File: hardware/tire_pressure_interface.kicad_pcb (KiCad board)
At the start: 2 copper layers, 98 x 40.1 mm, 82 parts, among them IC1 TPS54202HDDCR, J3 FTSH-107-01-L-D-K, J4 Conn_02x02_Counter_Clockwise, J5 Micro_SD_Card_Det1, Q1 SI2347DS-T1-GE3, T1 TP_+3V3, T10 TP_+5V, T11 TP_+5V, T3 TP_VCC, T8 TP_VCC, T9 TP_+3V3, U1 STM32G0C1KCTxN, U2 LM1117-3.3, U3 XIAO-ESP32-S3-DIP, U7 ADM3057ExRW

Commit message: pcb routing
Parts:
- moved T1 0.24 mm to (108.4, 114.0)
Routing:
- net GND: track 0.00 -> 115.7 mm, vias 0 -> 13
- net +3V3: track 0.00 -> 98.4 mm, vias 0 -> 13
- net /STM32/STM_VCC: track 0.00 -> 54.7 mm, vias 0 -> 5
- net /CAN_BUS/GND_CAN_ISO1: track 0.00 -> 51.2 mm, vias 0 -> 2
- net /Connectors/CAN.H: track 0.00 -> 48.2 mm
- net /Connectors/CAN.L: track 0.00 -> 47.8 mm
- net +5V: track 0.00 -> 46.8 mm
- net /TX: track 0.00 -> 45.5 mm, vias 0 -> 4
- net /RX: track 0.00 -> 44.6 mm, vias 0 -> 2
- net /Connectors/RST: track 0.00 -> 44.2 mm
- net /Power/VCC_IN: track 0.00 -> 43.3 mm, vias 0 -> 2
- net (no net): track 0.00 -> 38.1 mm
- net /CAN_BUS/CAN_RX: track 0.00 -> 32.8 mm
- net /CAN_BUS/STBY_CAN_1: track 0.00 -> 29.4 mm, vias 0 -> 2
- net /STM32/LED.ERR: track 0.00 -> 27.4 mm, vias 0 -> 2
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- added copper zone on B.Cu, net GND
- added copper zone on F.Cu, net GND

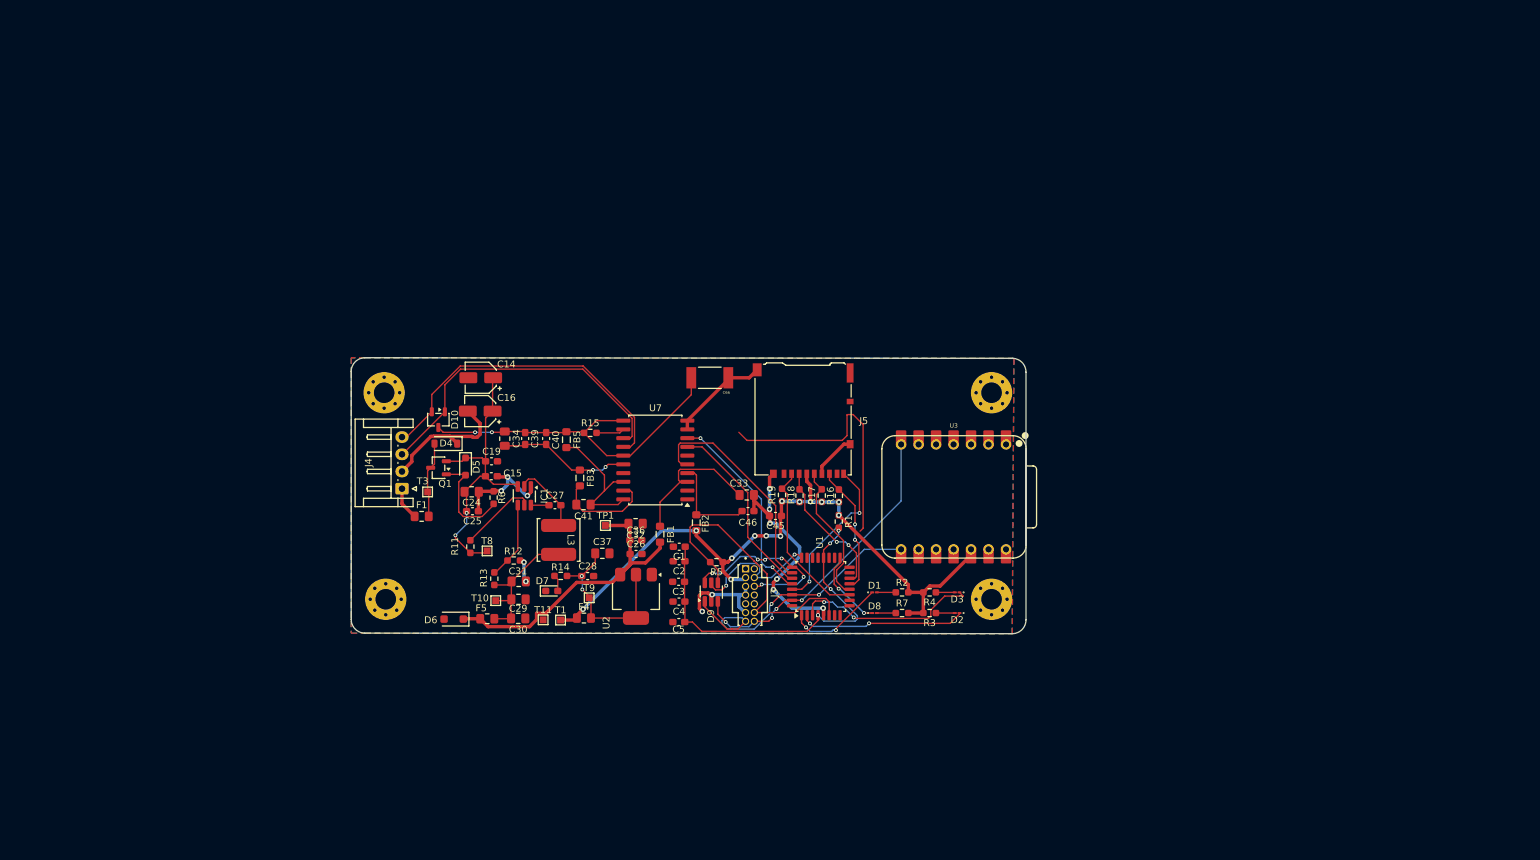
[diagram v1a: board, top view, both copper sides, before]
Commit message: power section routing
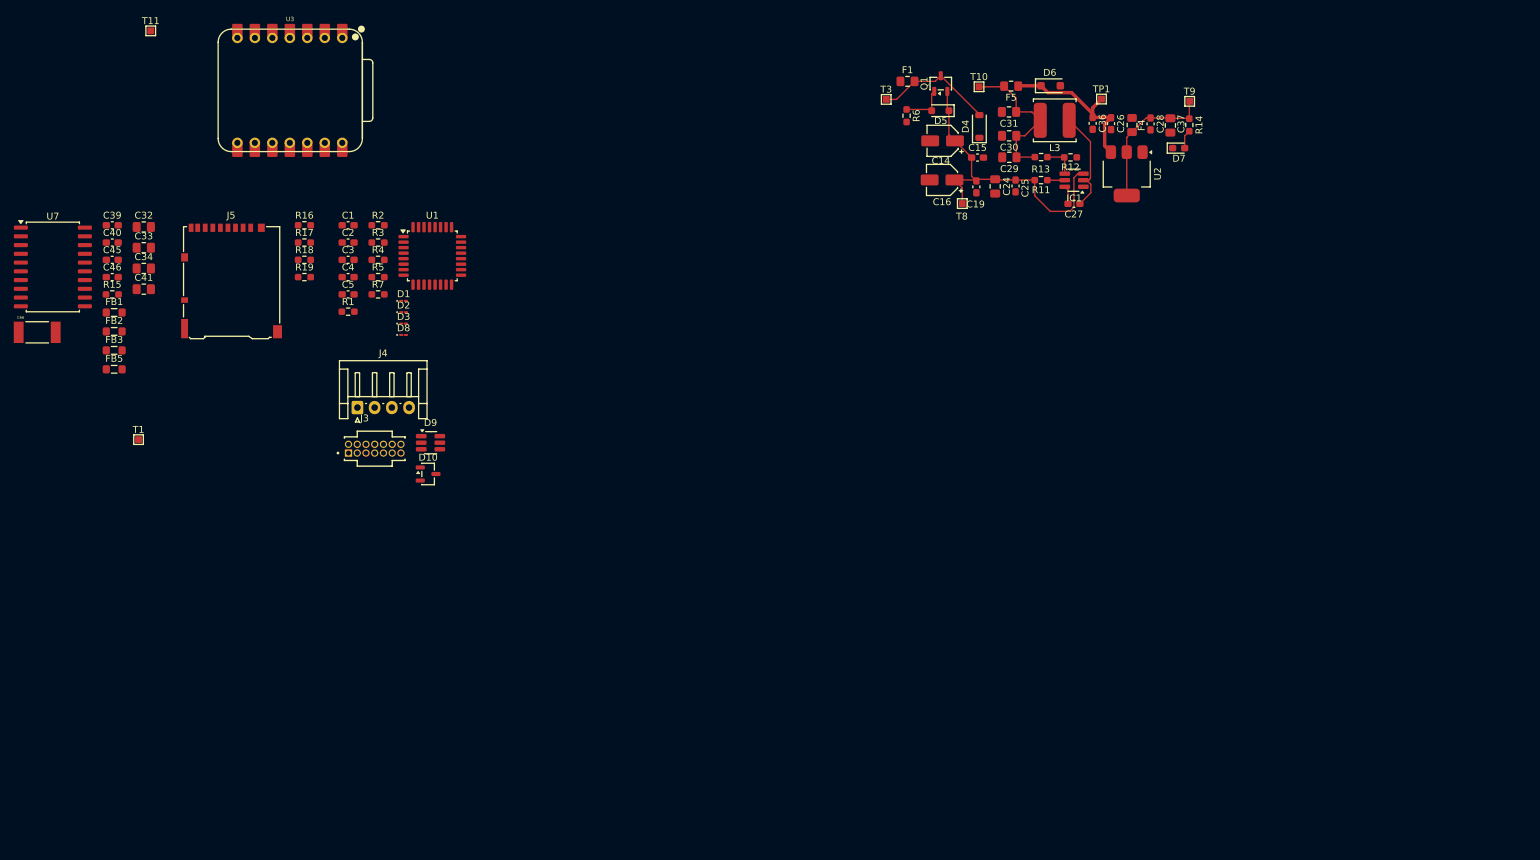
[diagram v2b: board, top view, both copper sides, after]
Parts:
- removed REF** (x4): MountingHole_3mm_Pad_Via, MountingHole:MountingHole_3mm_Pad_Via
- moved D6 116.3 mm to (179.6, 36.4), turned to 0 degrees
- moved T9 113.2 mm to (199.8, 38.7)
- moved U3 113.1 mm to (69.1, 37.1)
- moved R14 112.4 mm to (199.7, 42.1), turned to -90 degrees
- moved D7 111.5 mm to (198.2, 45.5)
- moved F5 108.5 mm to (173.8, 36.5), turned to 180 degrees
- moved F4 107.1 mm to (191.4, 42.1), turned to -90 degrees
- moved C28 104.9 mm to (194.1, 42.0), turned to -90 degrees
- moved C37 103.3 mm to (197.0, 42.2), turned to -90 degrees
- moved C45 103.3 mm to (43.3, 61.7), turned to 0 degrees
- moved T11 102.8 mm to (48.9, 28.4)
- moved T10 102.5 mm to (169.2, 36.6)
- moved R13 100.3 mm to (178.2, 46.8), turned to 180 degrees
- moved C30 100.0 mm to (173.6, 43.7), turned to 180 degrees
- moved R12 99.8 mm to (182.5, 46.8)
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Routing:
- net GND: track 115.7 -> 0.00 mm, vias 13 -> 0
- net +3V3: track 98.4 -> 0.00 mm, vias 13 -> 0
- net /STM32/STM_VCC: track 54.7 -> 0.00 mm, vias 5 -> 0
- net /CAN_BUS/GND_CAN_ISO1: track 51.2 -> 0.00 mm, vias 2 -> 0
- net /Connectors/CAN.H: track 48.2 -> 0.00 mm
- net /Connectors/CAN.L: track 47.8 -> 0.00 mm
- net /TX: track 45.5 -> 0.00 mm, vias 4 -> 0
- net /RX: track 44.6 -> 0.00 mm, vias 2 -> 0
- net /Connectors/RST: track 44.2 -> 0.00 mm
- net (no net): track 38.1 -> 0.00 mm
- net /CAN_BUS/CAN_RX: track 32.8 -> 0.00 mm
- net /CAN_BUS/STBY_CAN_1: track 29.4 -> 0.00 mm, vias 2 -> 0
- net /STM32/LED.ERR: track 27.4 -> 0.00 mm, vias 2 -> 0
- net /CAN_BUS/CAN_TX: track 26.9 -> 0.00 mm
- net /Connectors/SWCLK: track 25.8 -> 0.00 mm, vias 6 -> 0
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- removed copper zone on B.Cu, net GND
- removed copper zone on F.Cu, net GND
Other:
- board outline removed
- copper layers 2 -> 4

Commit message: power section and isocan layout
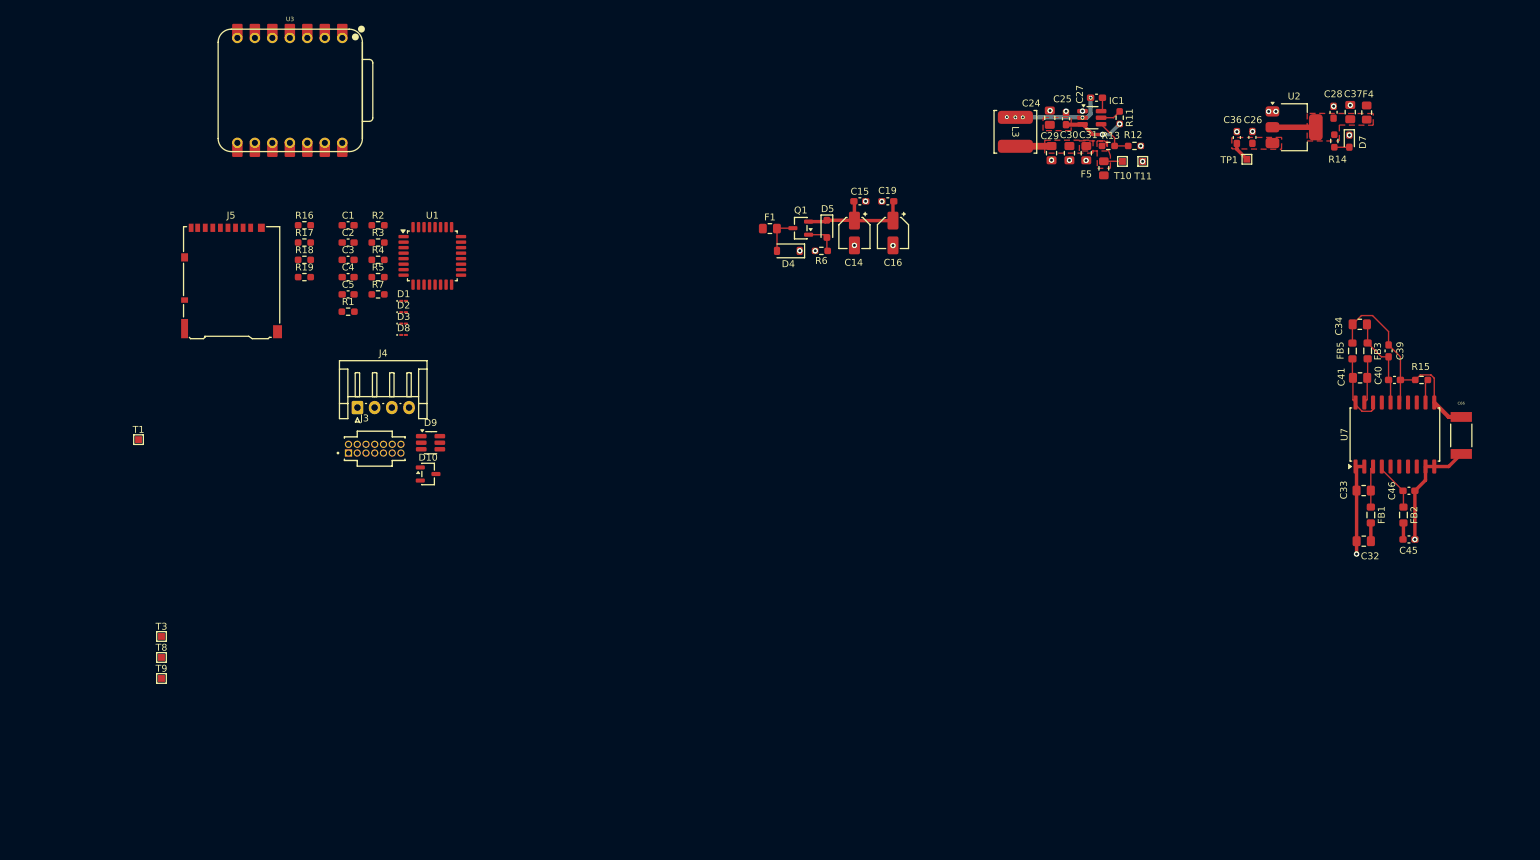
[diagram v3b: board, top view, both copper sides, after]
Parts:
- removed D6: SKL34, Diode_SMD:D_SOD-123F
- moved C66 207.4 mm to (239.2, 87.2), turned to 90 degrees
- moved U7 196.5 mm to (229.6, 87.1), turned to 90 degrees
- moved C45 192.7 mm to (231.6, 102.3)
- moved C46 190.9 mm to (231.6, 95.2)
- moved R15 190.6 mm to (233.5, 79.1)
- moved FB2 189.2 mm to (230.8, 98.8), turned to -90 degrees
- moved C40 187.3 mm to (229.5, 79.1)
- moved C39 186.3 mm to (228.7, 74.9), turned to -90 degrees
- moved FB1 184.9 mm to (226.1, 98.8), turned to -90 degrees
- moved C32 183.0 mm to (225.1, 102.6)
- moved FB3 182.1 mm to (225.6, 74.9), turned to -90 degrees
- moved C33 180.7 mm to (225.1, 95.2)
- moved FB5 179.9 mm to (223.4, 74.9), turned to -90 degrees
- moved C41 177.1 mm to (224.5, 78.8)
- moved C34 176.8 mm to (224.5, 71.1)
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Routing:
- net GND: track 0.00 -> 36.5 mm, vias 0 -> 23
- net /CAN_BUS/GND_CAN_ISO1: track 0.00 -> 34.3 mm
- net +5V: track 24.7 -> 5.56 mm
- net /Power/VCC_IN: track 45.6 -> 27.1 mm, vias 0 -> 2
- net /Power/+5V_OUT: track 23.0 -> 7.98 mm
- net /Power/VO_+3.3V: track 21.3 -> 6.36 mm
- net Net-(U7-VISOIN): track 0.00 -> 13.4 mm
- net /Power/RPP_D: track 17.4 -> 5.58 mm
- net Net-(C41-Pad1): track 0.00 -> 10.9 mm
- net Net-(U7-VIO): track 0.00 -> 7.20 mm
- net Net-(U7-VISOOUT): track 0.00 -> 6.55 mm
- net Net-(U7-VCC): track 0.00 -> 6.03 mm
- net Net-(U7-RS): track 0.00 -> 3.42 mm
- net +3V3: track 0.00 -> 2.43 mm
- net /Power/RPP_G: track 6.68 -> 4.82 mm
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- added copper zone on F.Cu, net +5V
- added copper zone on F.Cu, net /Power/+5V_OUT
- added copper zone on F.Cu, net /Power/VCC_IN
- added copper zone on F.Cu, net /Power/VO_+3.3V

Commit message: STM32G0 and micro sd layout
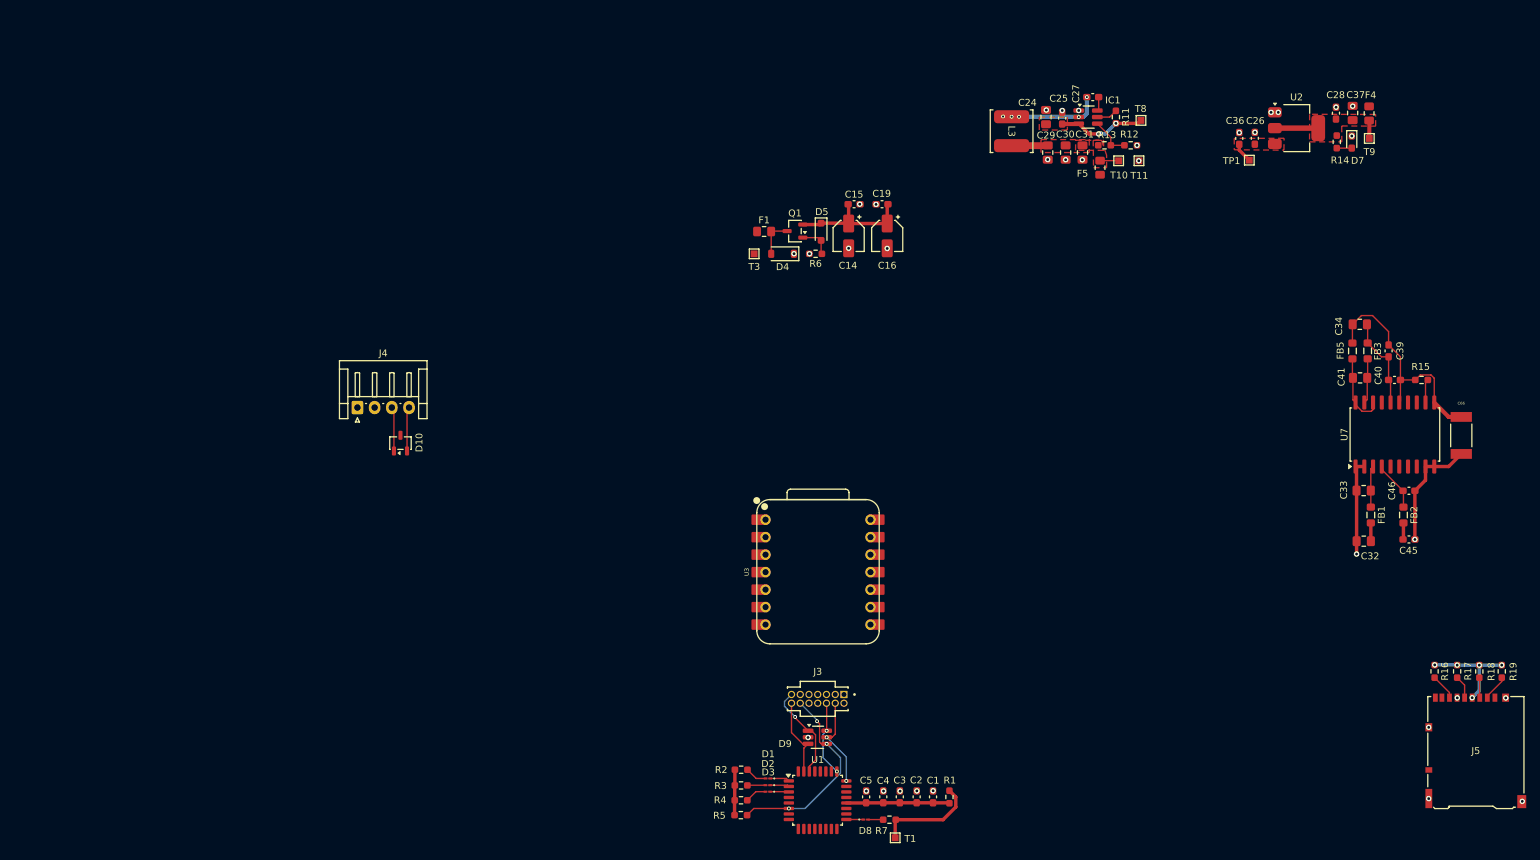
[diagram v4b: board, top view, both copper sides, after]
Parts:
- moved J5 193.2 mm to (241.3, 133.0)
- moved T9 192.2 mm to (225.9, 44.1)
- moved R19 183.1 mm to (245.1, 121.5), turned to -90 degrees
- moved R18 180.8 mm to (241.8, 121.5), turned to -90 degrees
- moved R17 178.7 mm to (238.6, 121.5), turned to -90 degrees
- moved R16 176.5 mm to (235.3, 121.5), turned to -90 degrees
- moved T8 162.3 mm to (192.7, 41.4)
- moved T1 124.2 mm to (157.0, 145.7)
- moved C1 118.8 mm to (162.5, 139.7), turned to 90 degrees
- moved C2 115.3 mm to (160.1, 139.7), turned to 90 degrees
- moved R1 112.2 mm to (164.9, 139.7), turned to -90 degrees
- moved C3 111.8 mm to (157.7, 139.7), turned to 90 degrees
- moved C4 108.4 mm to (155.3, 139.7), turned to 90 degrees
- moved R7 106.5 mm to (156.2, 143.0)
- moved C5 104.8 mm to (152.8, 139.7), turned to 90 degrees
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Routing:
- net +3V3: track 2.43 -> 38.9 mm, vias 0 -> 5
- net /Connectors/RST: track 0.00 -> 29.1 mm, vias 0 -> 3
- net /STM32/STM_VCC: track 0.00 -> 15.0 mm
- net /RX: track 0.00 -> 14.1 mm, vias 0 -> 1
- net /Connectors/SWDIO: track 0.00 -> 13.4 mm, vias 0 -> 2
- net /TX: track 0.00 -> 11.6 mm
- net /Connectors/SWCLK: track 0.00 -> 11.0 mm, vias 0 -> 2
- net /Connectors/CAN.L: track 0.00 -> 6.43 mm
- net /Connectors/CAN.H: track 0.00 -> 6.42 mm
- net /Power/VCC_IN: track 27.1 -> 30.9 mm
- net /Micro_SD_Card/MISO: track 0.00 -> 3.80 mm
- net /Micro_SD_Card/NSS: track 0.00 -> 3.78 mm
- net /STM32/LED.WRN: track 0.00 -> 3.55 mm
- net /Micro_SD_Card/SCK: track 0.00 -> 3.36 mm
- net /STM32/LD_ER_R: track 0.00 -> 3.16 mm
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
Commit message: routing and PCB outline
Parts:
- added REF**: MountingHole_3.2mm_M3_Pad_Via, REST:MountingHole_3.2mm_M3_Pad_Via, F.Cu at (75.3, 133.8)
- added REF**: MountingHole_3.2mm_M3_Pad_Via, REST:MountingHole_3.2mm_M3_Pad_Via, F.Cu at (144.5, 133.8)
- added REF**: MountingHole_3.2mm_M3_Pad_Via, REST:MountingHole_3.2mm_M3_Pad_Via, F.Cu at (144.5, 79.3)
- added REF**: MountingHole_3.2mm_M3_Pad_Via, REST:MountingHole_3.2mm_M3_Pad_Via, F.Cu at (75.3, 79.3)
- moved C28 129.7 mm to (118.8, 120.2)
- moved T9 129.7 mm to (123.6, 123.8)
- moved TP1 129.7 mm to (106.2, 127.0)
- moved C26 129.7 mm to (107.0, 123.8)
- moved C36 129.7 mm to (104.7, 123.8)
- moved C37 129.7 mm to (121.2, 120.1)
- moved D7 129.7 mm to (121.1, 124.4)
- moved F4 129.7 mm to (123.6, 120.2)
- moved R14 129.7 mm to (118.9, 124.3)
- moved U2 129.7 mm to (113.1, 122.3)
- moved C33 124.8 mm to (100.5, 102.6)
- moved C34 124.8 mm to (99.9, 78.4)
- moved C40 124.8 mm to (105.0, 86.5)
- moved C41 124.8 mm to (100.0, 86.2)
- moved FB1 124.8 mm to (101.5, 106.1)
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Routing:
- net +3V3: track 38.9 -> 160.3 mm, vias 5 -> 7
- net /Micro_SD_Card/DET: track 0.00 -> 33.4 mm
- net +5V: track 5.56 -> 31.2 mm
- net /TX: track 11.6 -> 37.1 mm, vias 0 -> 1
- net /CAN_BUS/CAN_RX: track 0.00 -> 25.1 mm, vias 0 -> 2
- net /CAN_BUS/CAN_TX: track 0.00 -> 22.2 mm, vias 0 -> 2
- net /CAN_BUS/STBY_CAN_1: track 0.00 -> 22.1 mm, vias 0 -> 4
- net /Connectors/CAN.L: track 6.43 -> 27.3 mm
- net /Micro_SD_Card/MISO: track 3.80 -> 21.6 mm
- net /Connectors/CAN.H: track 6.42 -> 23.8 mm
- net /Micro_SD_Card/SCK: track 3.36 -> 20.6 mm, vias 0 -> 2
- net /CAN_BUS/GND_CAN_ISO1: track 34.3 -> 48.5 mm
- net /RX: track 14.1 -> 27.5 mm, vias 1 -> 0
- net /Micro_SD_Card/NSS: track 3.78 -> 16.7 mm
- net /Connectors/RST: track 29.1 -> 41.7 mm, vias 3 -> 2
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- added copper zone on In1.Cu, net GND
- added copper zone on In2.Cu, net GND
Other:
- board outline added: 80.2 x 65.5 mm
